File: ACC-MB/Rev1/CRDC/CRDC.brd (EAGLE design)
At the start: 180 x 64 mm, 7 parts

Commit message: update
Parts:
- removed U$5: TO247RESISTORHEATINK, ACC-MB-R0:_CUSTOM_TO-247-2V
- added LED1, LED2: (no value), ACC-MB-R0:LED3MM
- added R1, R2: (no value), ACC-MB-R0:TO-247-2H
- added R3, R4: (no value), ACC-MB-R0:R0805
- added U$8, U$9: HEATSINK40X40X15, ACC-MB-R0:HEATSINK40X40X15
- U$3: value TO247RESISTORHEATINK -> BENDER_IRR155; device ACC-MB-R0:_CUSTOM_TO-247-2V -> ACC-MB-R0:BENDER_IRR155
- moved U$3 90.3 mm to (50.0, 60.0), flipped to the bottom, turned to 180 degrees
- moved U$7 17.7 mm to (153.1, 5.24), turned to 180 degrees
- moved U$2 11.0 mm to (109.0, 61.0), flipped to the bottom
- moved U$1 10.0 mm to (87.0, 61.0), flipped to the bottom
- moved U$4 6.00 mm to (35.0, 18.0)
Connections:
- net HV-_DRY renamed HV-_DRY_AUX
- new net N$1: LED2.K, R3.2
- new net N$5: LED1.K, R4.2
- net DISCHARGE: now also LED2.A
- net GND: now also R3.1, R4.1
- net HV+_DRY: now also R2.1; no longer U$3.2
- net HV+_WET: now also R1.1; no longer U$5.2
- net N$21: now also R1.2; no longer U$5.1
- net N$4: now also R2.2; no longer U$3.1
- net PRECHARGE: now also LED1.A
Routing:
- net +12V: track 21.7 -> 50.2 mm
- net PRECHARGE: track 85.1 -> 111.0 mm
- net PRECHARGE_SIG: track 37.9 -> 51.2 mm
- net HV+_DRY: track 150.8 -> 138.6 mm
- net HV+_WET: track 46.7 -> 35.2 mm
- net N$21: track 34.5 -> 24.2 mm
- net HV-_DRY_AUX: track 112.4 -> 120.2 mm
- net DISCHARGE: track 95.7 -> 103.2 mm
- net N$1: track 0.00 -> 4.13 mm
- net N$5: track 0.00 -> 3.13 mm
- net N$4: track 23.0 -> 26.1 mm
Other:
- board size 180 x 64 mm -> 174 x 64 mm

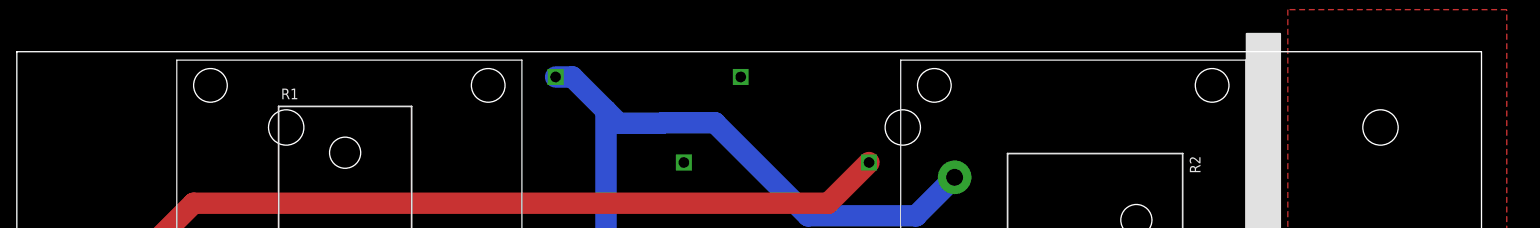
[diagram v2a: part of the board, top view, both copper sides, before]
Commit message: 7792 added to all DC
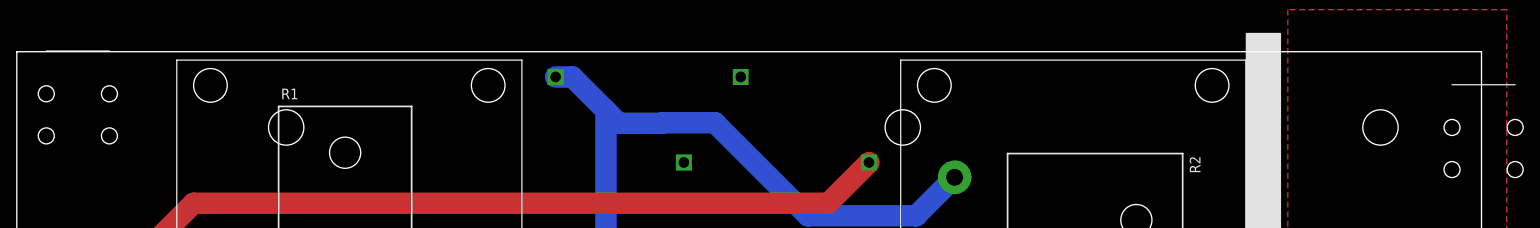
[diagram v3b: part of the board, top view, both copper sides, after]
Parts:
- added U$10, U$5: 7792, ACC-MB-R0:7792
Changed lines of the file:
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@@
 <drawing>
 <settings>
-<setting alwaysvectorfont="yes"/>
+<setting alwaysvectorfont="no"/>
 <setting verticaltext="up"/>
 </settings>
@@
 </element>
 <element name="U$3" library="ACC-MB-R0" library_urn="urn:adsk.eagle:library:13208985" package="BENDER_IRR155" package3d_urn="urn:adsk.eagle:package:14400200/2" value="BENDER_IRR155" x="50" y="60" rot="MR180"/>
+<element name="U$5" library="ACC-MB-R0" library_urn="urn:adsk.eagle:library:13208985" package="7792" package3d_urn="urn:adsk.eagle:package:14511284/2" value="7792" x="26.5" y="54"/>
+<element name="U$10" library="ACC-MB-R0" library_urn="urn:adsk.eagle:library:13208985" package="7792" package3d_urn="urn:adsk.eagle:package:14511284/2" value="7792" x="193.5" y="50"/>
 </elements>
 <signals>
